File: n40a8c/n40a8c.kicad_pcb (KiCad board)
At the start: 2 copper layers, 267.9 x 104.9 mm, 111 parts, among them J1 Conn_01x02_Pin, J2 Conn_01x02_Pin, SW1 CPG151101S11-16, SW10 CPG151101S11-16, SW11 CPG151101S11-16, SW12 CPG151101S11-16, SW13 CPG151101S11-16, SW14 CPG151101S11-16, SW15 CPG151101S11-16, SW16 CPG151101S11-16, SW17 CPG151101S11-16, SW18 CPG151101S11-16, SW19 CPG151101S11-16, SW2 CPG151101S11-16, SW20 CPG151101S11-16, SW21 CPG151101S11-16, SW22 CPG151101S11-16, SW23 CPG151101S11-16, SW24 CPG151101S11-16, SW25 CPG151101S11-16, SW26 CPG151101S11-16, SW27 CPG151101S11-16, SW28 CPG151101S11-16, SW29 CPG151101S11-16, SW3 CPG151101S11-16, SW30 CPG151101S11-16, SW31 CPG151101S11-16, SW32 CPG151101S11-16, SW33 CPG151101S11-16, SW34 CPG151101S11-16, SW35 CPG151101S11-16, SW36 CPG151101S11-16, SW37 CPG151101S11-16, SW38 CPG151101S11-16, SW39 CPG151101S11-16, SW4 CPG151101S11-16, SW40 CPG151101S11-16, SW41 CPG151101S11-16, SW42 CPG151101S11-16, SW5 CPG151101S11-16, SW6 CPG151101S11-16, SW7 CPG151101S11-16, SW8 CPG151101S11-16, SW9 CPG151101S11-16, U1 XIAO-nRF52840-SMD

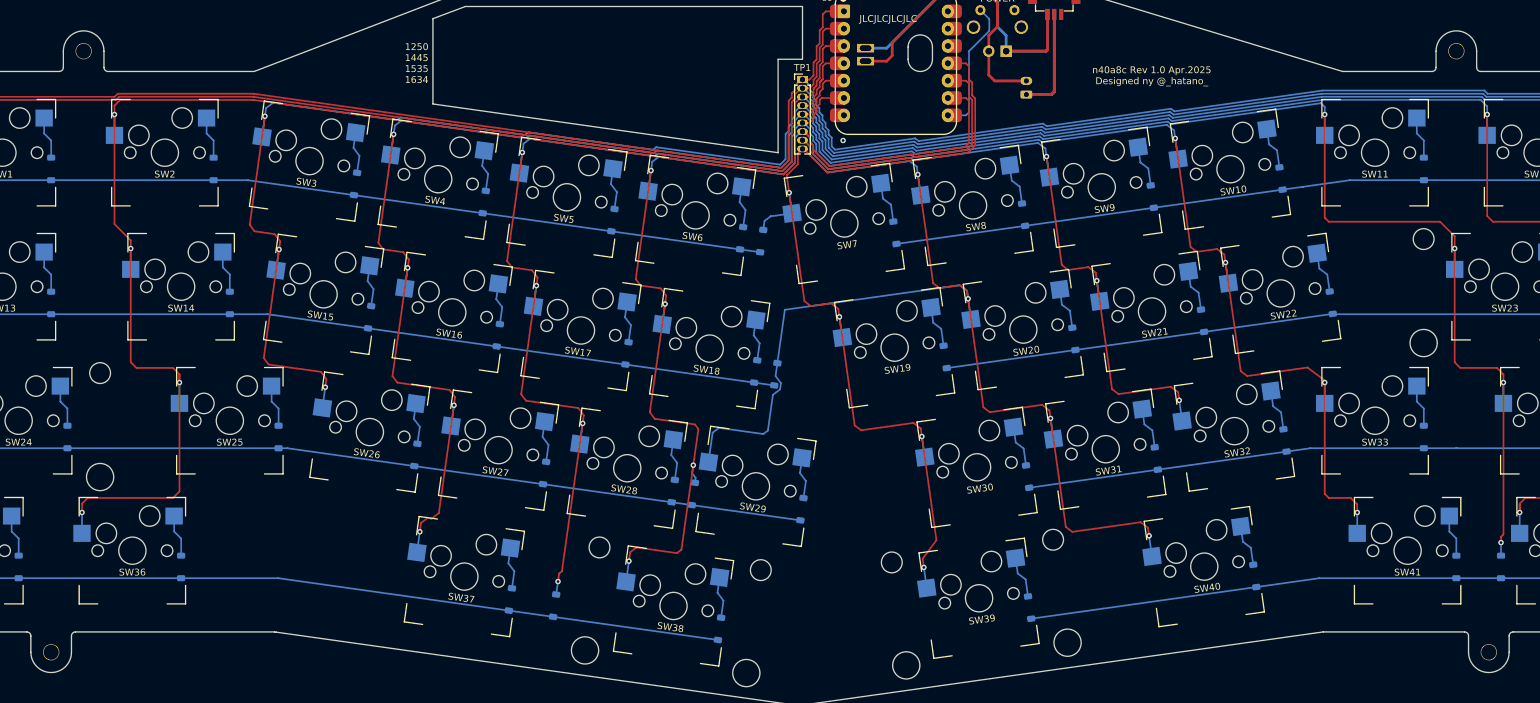
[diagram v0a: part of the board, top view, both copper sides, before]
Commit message: M2→M2.6
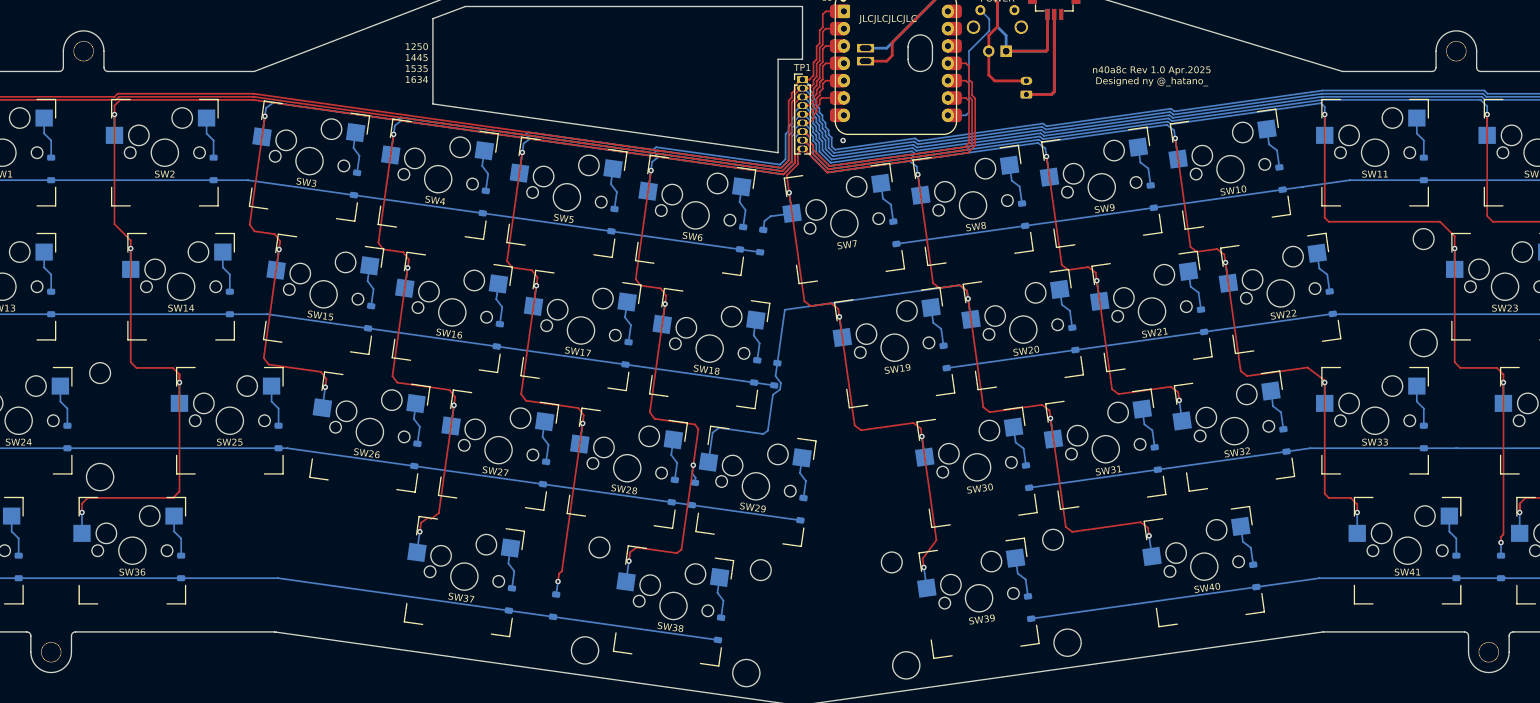
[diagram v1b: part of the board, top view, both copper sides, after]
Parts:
- H1, H2, H3, H4: footprint cscslib:MountingHole_M2_plating -> cscslib:MountingHole_M2.6_plating

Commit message: M2.6→M3
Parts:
- H1, H2, H3, H4: footprint cscslib:MountingHole_M2.6_plating -> cscslib:MountingHole_M3_plating_truss
- moved H1 1.19 mm to (45.2, 31.6)
- moved H2 1.19 mm to (246.5, 31.6)
- moved H3 1.19 mm to (40.5, 122.0)
- moved H4 1.19 mm to (251.2, 122.0)
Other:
- outline, holes or cut-outs redrawn

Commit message: revice tab
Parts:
- moved H1 2.98 mm to (45.2, 28.6)
- moved H3 2.98 mm to (40.5, 125.0)
- moved H4 2.98 mm to (251.2, 125.0)
- moved H2 2.98 mm to (246.5, 28.6)
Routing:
- net IO 3: track 289.5 -> 290.7 mm
- net IO 4: track 341.2 -> 341.9 mm
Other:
- outline, holes or cut-outs redrawn

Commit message: revise tab
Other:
- outline, holes or cut-outs redrawn
- board text added: "L-origin"
- board text removed: "L-Origin"

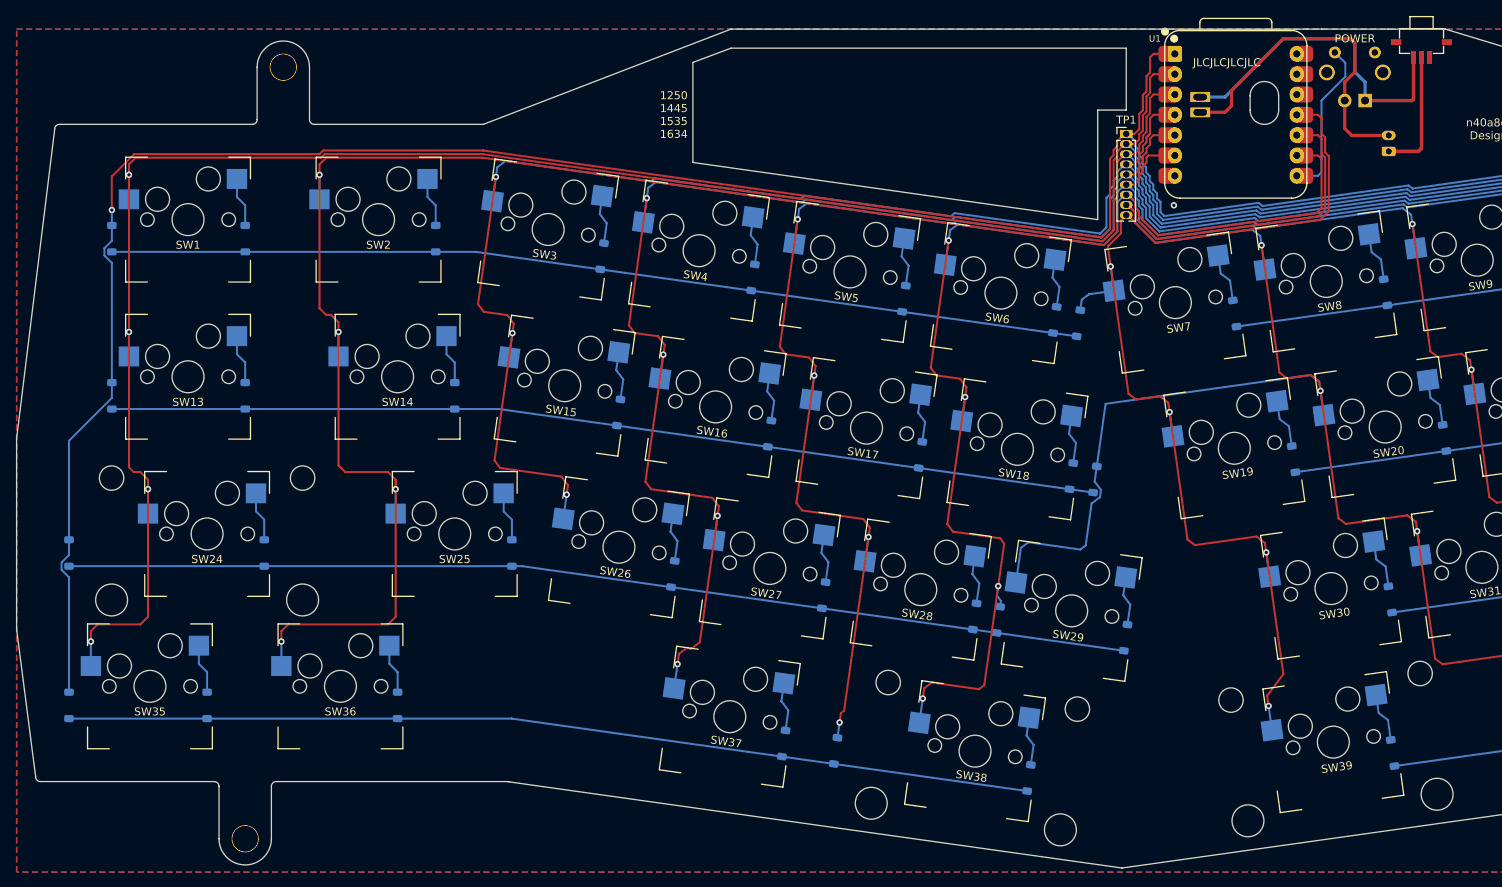
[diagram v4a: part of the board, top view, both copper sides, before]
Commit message: comply design rule (JLCPCB)
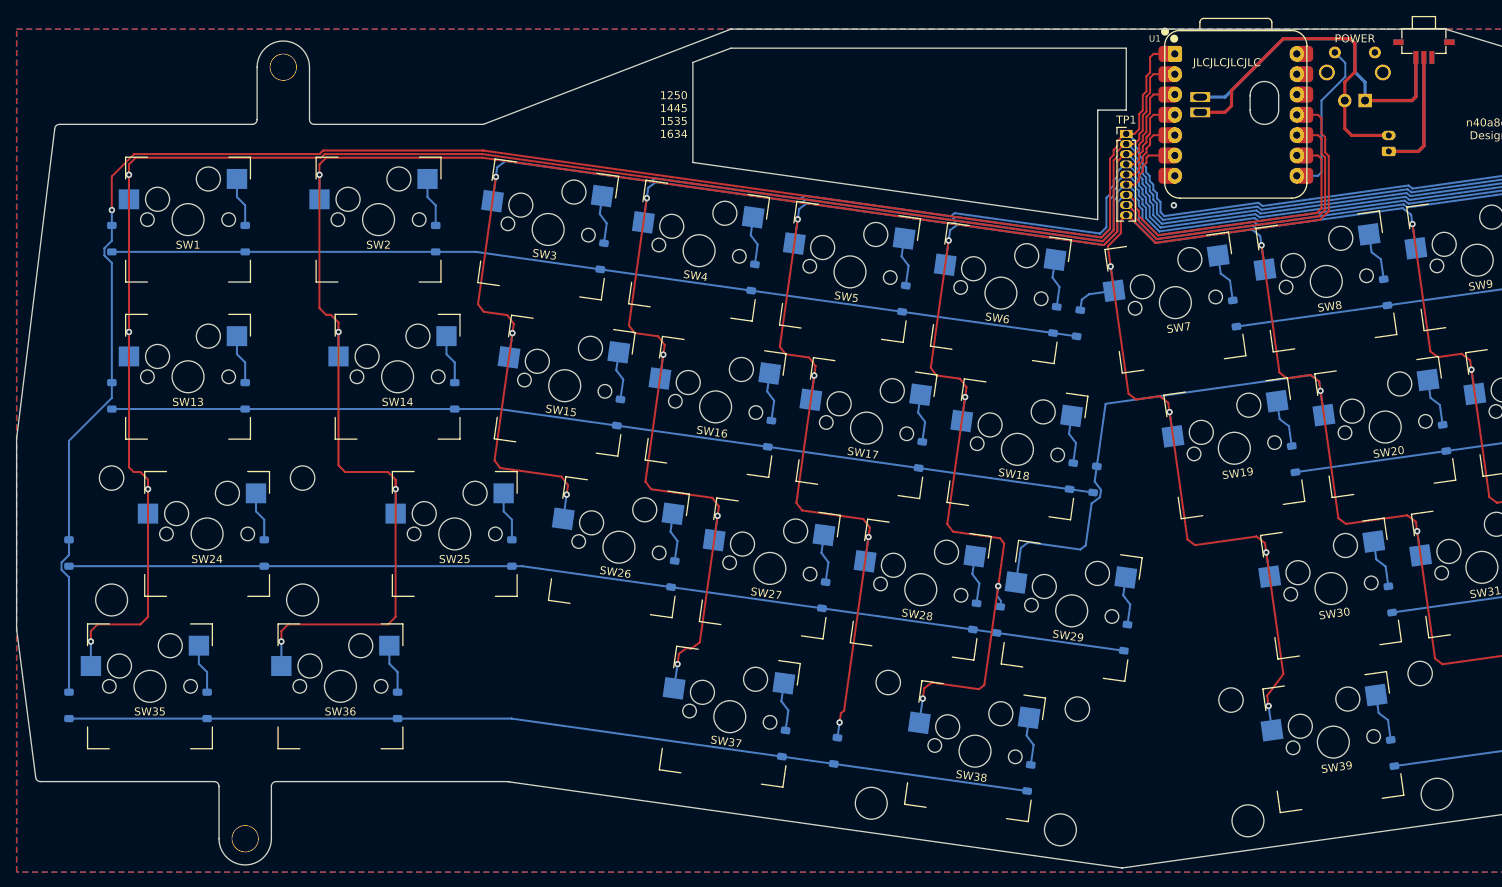
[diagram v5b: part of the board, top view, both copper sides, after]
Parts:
- moved SW_HPWR1 0.30 mm to (187.8, 25.6)
- moved SW_HPWR2 0.30 mm to (187.8, 25.6)
